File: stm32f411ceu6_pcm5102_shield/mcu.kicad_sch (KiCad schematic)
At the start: 25 parts, among them J3 Conn_01x04_Pin, J4 Conn_01x04_Pin, SW1 RotaryEncoder_Switch_MP

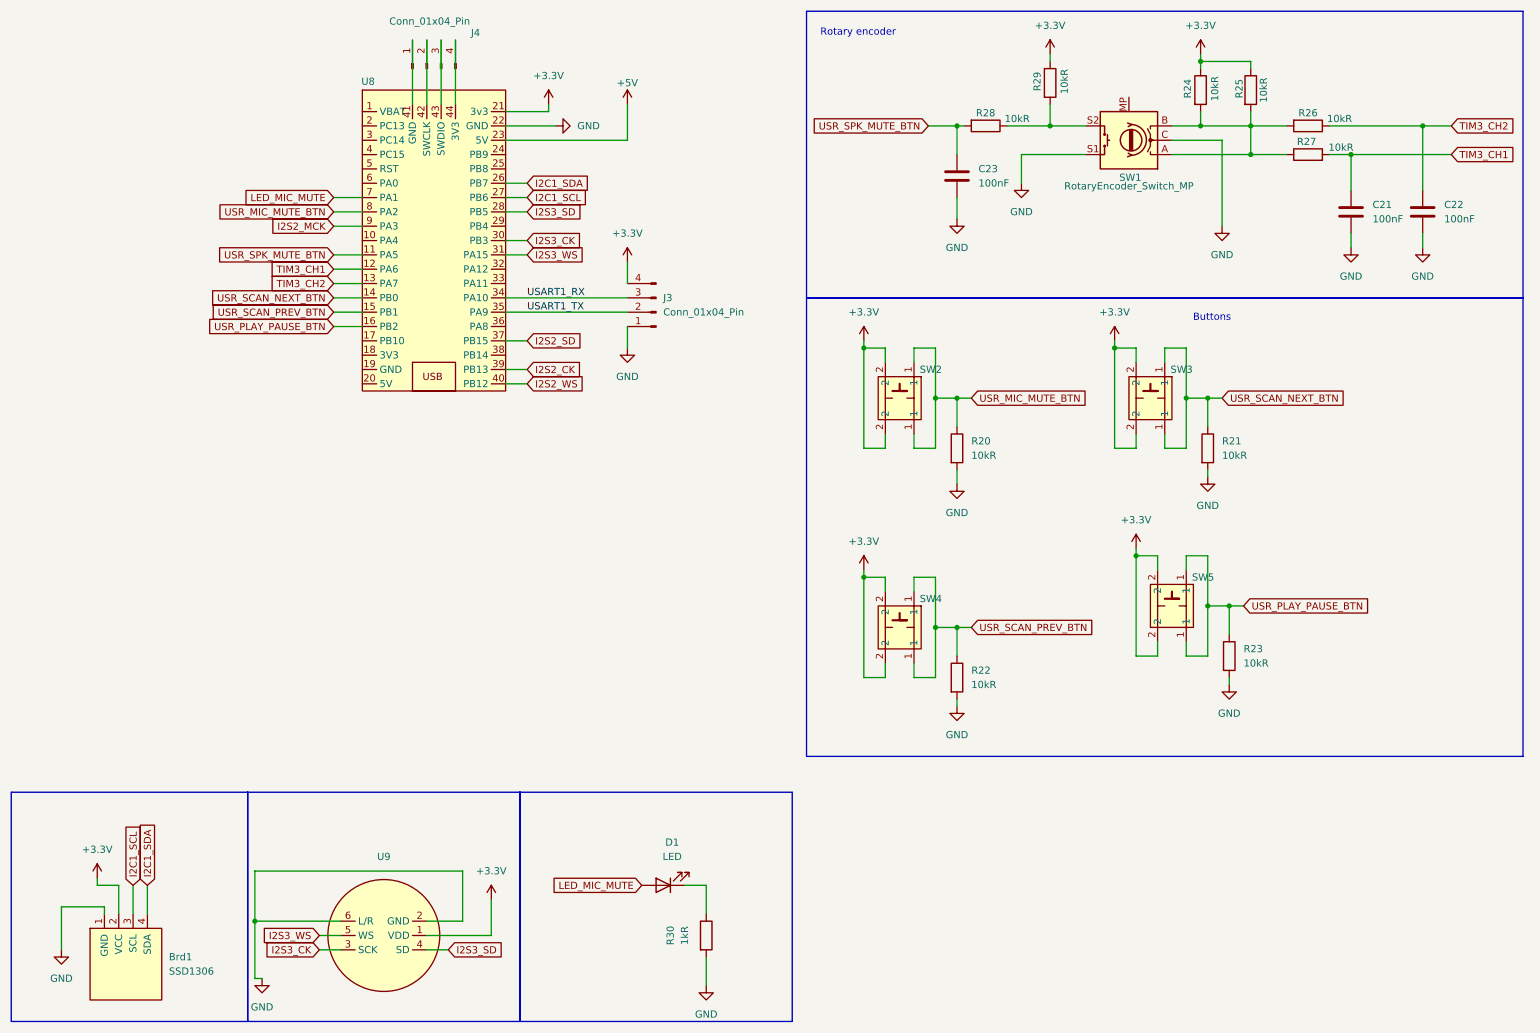
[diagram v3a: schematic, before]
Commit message: Items numeration fix
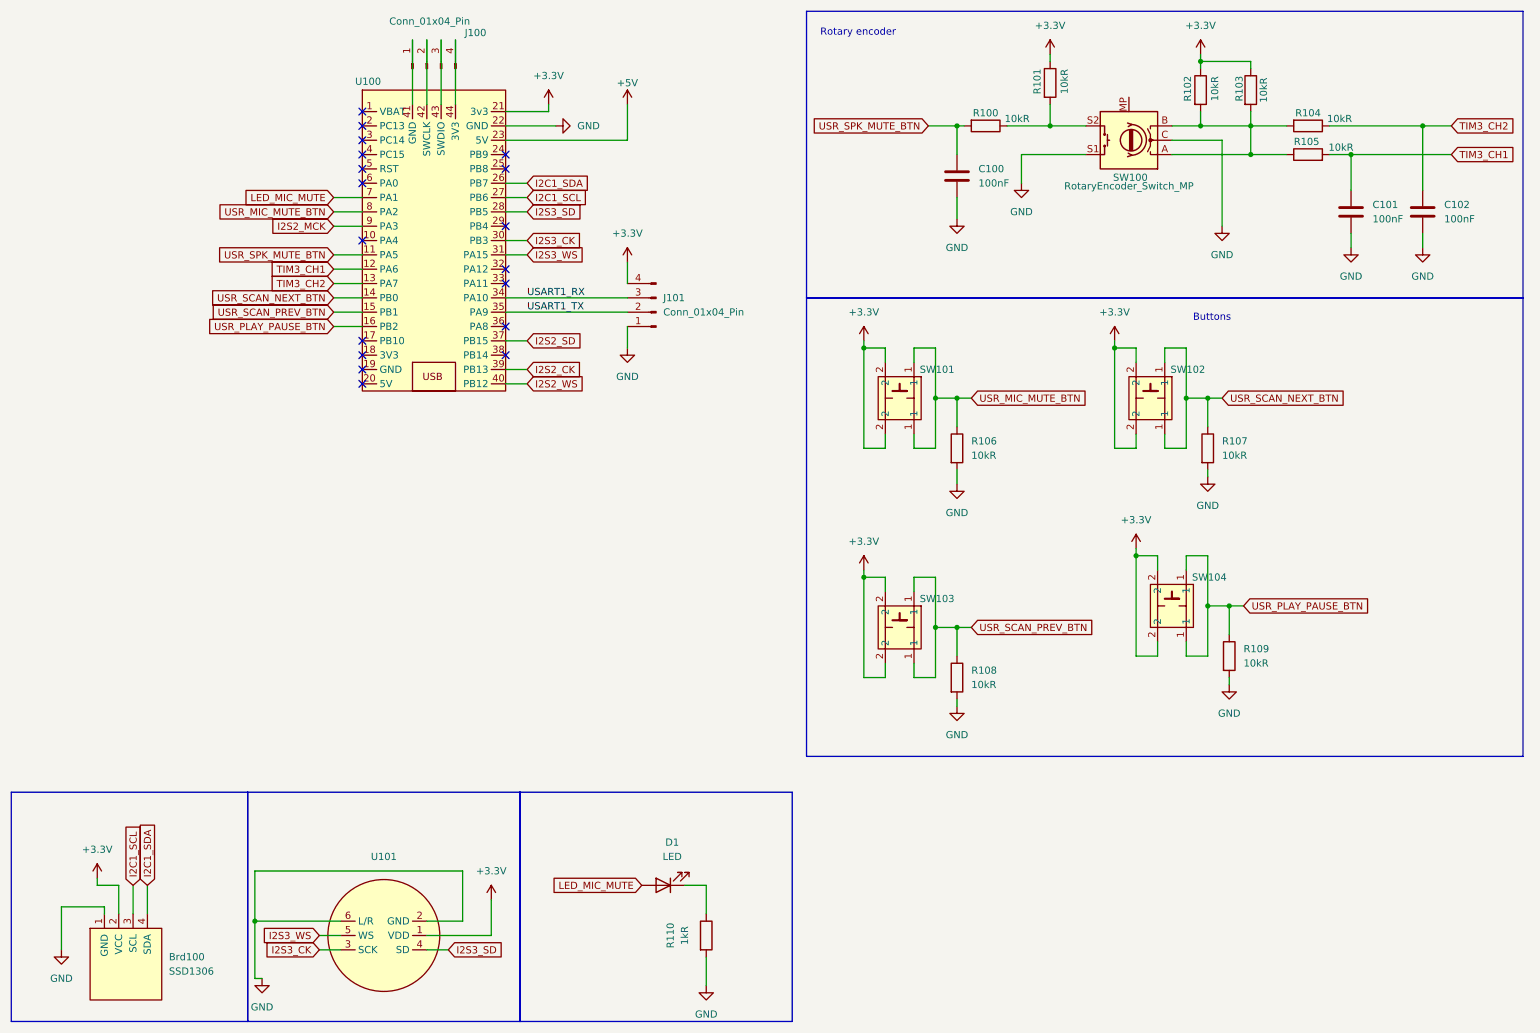
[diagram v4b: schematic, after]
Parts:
- renumbered Brd1 to Brd100, C23 to C100, C21 to C101, C22 to C102, J4 to J100, J3 to J101, R28 to R100, R29 to R101, R24 to R102, R25 to R103, R26 to R104, R27 to R105, R20 to R106, R21 to R107, R22 to R108, R23 to R109, R30 to R110, SW1 to SW100, SW2 to SW101, SW3 to SW102, SW4 to SW103, SW5 to SW104, U8 to U100, U9 to U101
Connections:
- no-connect marks 0 -> 18
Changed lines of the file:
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@@
 		(color 0 0 0 0)
 	)
+	(no_connect
+		(at 74.93 40.64)
+	)
+	(no_connect
+		(at 74.93 78.74)
+	)
+	(no_connect
+		(at 100.33 63.5)
+	)
+	(no_connect
+		(at 74.93 81.28)
+	)
+	(no_connect
+		(at 100.33 60.96)
+	)
+	(no_connect
+		(at 74.93 76.2)
+	)
+	(no_connect
+		(at 74.93 55.88)
+	)
+	(no_connect
+		(at 74.93 35.56)
+	)
+	(no_connect
+		(at 100.33 71.12)
+	)
+	(no_connect
+		(at 74.93 43.18)
+	)
+	(no_connect
+		(at 100.33 76.2)
+	)
+	(no_connect
+		(at 74.93 45.72)
+	)
+	(no_connect
+		(at 74.93 73.66)
+	)
+	(no_connect
+		(at 74.93 33.02)
+	)
+	(no_connect
+		(at 100.33 40.64)
+	)
+	(no_connect
+		(at 100.33 43.18)
+	)
+	(no_connect
+		(at 74.93 38.1)
+	)
+	(no_connect
+		(at 100.33 53.34)
+	)
 	(wire
 		(pts
@@
 		(on_board yes)
 		(dnp no)
-		(property "Reference" "R30"
+		(property "Reference" "R110"
 			(at 129.54 179.07 90)
 			(effects
@@
 			(project "stm32f411ceu6_pcm5102_shield"
 				(path "/aeaad843-2b7c-40e9-bb1d-8d1f5e5d5206/850fb9da-5125-4af4-b1b4-d624ecc42efc"
-					(reference "R30")
+					(reference "R110")
 					(unit 1)
 				)
@@
 		(dnp no)
 		(fields_autoplaced yes)
-		(property "Reference" "R20"
+		(property "Reference" "R106"
 			(at 182.88 91.4399 0)
 			(effects
@@
 			(project "stm32f411ceu6_pcm5102_shield"
 				(path "/aeaad843-2b7c-40e9-bb1d-8d1f5e5d5206/850fb9da-5125-4af4-b1b4-d624ecc42efc"
-					(reference "R20")
+					(reference "R106")
 					(unit 1)
 				)
@@
 		(on_board yes)
 		(dnp no)
-		(property "Reference" "SW4"
+		(property "Reference" "SW103"
 			(at 173.736 119.38 90)
 			(effects
@@
 			(project "stm32f411ceu6_pcm5102_shield"
 				(path "/aeaad843-2b7c-40e9-bb1d-8d1f5e5d5206/850fb9da-5125-4af4-b1b4-d624ecc42efc"
-					(reference "SW4")
+					(reference "SW103")
 					(unit 1)
 				)
@@
 		(on_board yes)
 		(dnp no)
-		(property "Reference" "SW3"
+		(property "Reference" "SW102"
 			(at 218.186 78.74 90)
 			(effects
@@
 			(project "stm32f411ceu6_pcm5102_shield"
 				(path "/aeaad843-2b7c-40e9-bb1d-8d1f5e5d5206/850fb9da-5125-4af4-b1b4-d624ecc42efc"
-					(reference "SW3")
+					(reference "SW102")
 					(unit 1)
 				)
@@
 		(on_board yes)
 		(dnp no)
-		(property "Reference" "J4"
+		(property "Reference" "J100"
 			(at 94.996 19.05 90)
 			(effects
@@
 			(project "stm32f411ceu6_pcm5102_shield"
 				(path "/aeaad843-2b7c-40e9-bb1d-8d1f5e5d5206/850fb9da-5125-4af4-b1b4-d624ecc42efc"
-					(reference "J4")
+					(reference "J100")
 					(unit 1)
 				)
@@
 		(on_board yes)
 		(dnp no)
-		(property "Reference" "U8"
+		(property "Reference" "U100"
 			(at 75.946 27.686 0)
 			(effects
@@
 			(project ""
 				(path "/aeaad843-2b7c-40e9-bb1d-8d1f5e5d5206/850fb9da-5125-4af4-b1b4-d624ecc42efc"
-					(reference "U8")
+					(reference "U100")
 					(unit 1)
 				)
@@
 		(on_board yes)
 		(dnp no)
-		(property "Reference" "R27"
+		(property "Reference" "R105"
 			(at 242.316 38.354 90)
 			(effects
@@
 			(project "stm32f411ceu6_pcm5102_shield"
 				(path "/aeaad843-2b7c-40e9-bb1d-8d1f5e5d5206/850fb9da-5125-4af4-b1b4-d624ecc42efc"
-					(reference "R27")
+					(reference "R105")
 					(unit 1)
 				)
@@
 		(on_board yes)
 		(dnp no)
-		(property "Reference" "SW1"
+		(property "Reference" "SW100"
 			(at 211.074 44.704 0)
 			(effects
@@
 			(project ""
 				(path "/aeaad843-2b7c-40e9-bb1d-8d1f5e5d5206/850fb9da-5125-4af4-b1b4-d624ecc42efc"
-					(reference "SW1")
+					(reference "SW100")
 					(unit 1)
 				)
@@
 		(on_board yes)
 		(dnp no)
-		(property "Reference" "C23"
+		(property "Reference" "C100"
 			(at 184.15 43.18 0)
 			(effects
@@
 			(project "stm32f411ceu6_pcm5102_shield"
 				(path "/aeaad843-2b7c-40e9-bb1d-8d1f5e5d5206/850fb9da-5125-4af4-b1b4-d624ecc42efc"
-					(reference "C23")
+					(reference "C100")
 					(unit 1)
 				)
@@
 		(dnp no)
 		(fields_autoplaced yes)
-		(property "Reference" "R22"
+		(property "Reference" "R108"
 			(at 182.88 132.0799 0)
 			(effects
@@
 			(project "stm32f411ceu6_pcm5102_shield"
 				(path "/aeaad843-2b7c-40e9-bb1d-8d1f5e5d5206/850fb9da-5125-4af4-b1b4-d624ecc42efc"
-					(reference "R22")
+					(reference "R108")
 					(unit 1)
 				)
@@
 		(on_board yes)
 		(dnp no)
-		(property "Reference" "R25"
+		(property "Reference" "R103"
 			(at 230.378 28.956 90)
 			(effects
@@
 			(project "stm32f411ceu6_pcm5102_shield"
 				(path "/aeaad843-2b7c-40e9-bb1d-8d1f5e5d5206/850fb9da-5125-4af4-b1b4-d624ecc42efc"
-					(reference "R25")
+					(reference "R103")
 					(unit 1)
 				)
@@
 		(on_board yes)
 		(dnp no)
-		(property "Reference" "R29"
+		(property "Reference" "R101"
 			(at 194.564 27.686 90)
 			(effects
@@
 			(project "stm32f411ceu6_pcm5102_shield"
 				(path "/aeaad843-2b7c-40e9-bb1d-8d1f5e5d5206/850fb9da-5125-4af4-b1b4-d624ecc42efc"
-					(reference "R29")
+					(reference "R101")
 					(unit 1)
 				)
@@
 		(on_board yes)
 		(dnp no)
-		(property "Reference" "C21"
+		(property "Reference" "C101"
 			(at 254 49.53 0)
 			(effects
@@
 			(project "stm32f411ceu6_pcm5102_shield"
 				(path "/aeaad843-2b7c-40e9-bb1d-8d1f5e5d5206/850fb9da-5125-4af4-b1b4-d624ecc42efc"
-					(reference "C21")
+					(reference "C101")
 					(unit 1)
 				)
@@
 		(dnp no)
 		(fields_autoplaced yes)
-		(property "Reference" "J3"
+		(property "Reference" "J101"
 			(at 128.27 66.0399 0)
 			(effects
@@
 			(project ""
 				(path "/aeaad843-2b7c-40e9-bb1d-8d1f5e5d5206/850fb9da-5125-4af4-b1b4-d624ecc42efc"
-					(reference "J3")
+					(reference "J101")
 					(unit 1)
 				)
@@
 		(on_board yes)
 		(dnp no)
-		(property "Reference" "R28"
+		(property "Reference" "R100"
 			(at 185.42 33.274 90)
 			(effects
@@
 			(project "stm32f411ceu6_pcm5102_shield"
 				(path "/aeaad843-2b7c-40e9-bb1d-8d1f5e5d5206/850fb9da-5125-4af4-b1b4-d624ecc42efc"
-					(reference "R28")
+					(reference "R100")
 					(unit 1)
 				)
@@
 		(on_board yes)
 		(dnp no)
-		(property "Reference" "SW2"
+		(property "Reference" "SW101"
 			(at 173.736 78.74 90)
 			(effects
@@
 			(project "stm32f411ceu6_pcm5102_shield"
 				(path "/aeaad843-2b7c-40e9-bb1d-8d1f5e5d5206/850fb9da-5125-4af4-b1b4-d624ecc42efc"
-					(reference "SW2")
+					(reference "SW101")
 					(unit 1)
 				)
@@
 		(dnp no)
 		(fields_autoplaced yes)
-		(property "Reference" "Brd1"
+		(property "Reference" "Brd100"
 			(at 40.64 182.8799 0)
 			(effects
@@
 			(project ""
 				(path "/aeaad843-2b7c-40e9-bb1d-8d1f5e5d5206/850fb9da-5125-4af4-b1b4-d624ecc42efc"
-					(reference "Brd1")
+					(reference "Brd100")
 					(unit 1)
 				)
@@
 		(dnp no)
 		(fields_autoplaced yes)
-		(property "Reference" "R23"
+		(property "Reference" "R109"
 			(at 231.14 128.2699 0)
 			(effects
@@
 			(project "stm32f411ceu6_pcm5102_shield"
 				(path "/aeaad843-2b7c-40e9-bb1d-8d1f5e5d5206/850fb9da-5125-4af4-b1b4-d624ecc42efc"
-					(reference "R23")
+					(reference "R109")
 					(unit 1)
 				)
@@
 		(dnp no)
 		(fields_autoplaced yes)
-		(property "Reference" "U9"
+		(property "Reference" "U101"
 			(at 78.74 165.1 0)
 			(effects
@@
 			(project ""
 				(path "/aeaad843-2b7c-40e9-bb1d-8d1f5e5d5206/850fb9da-5125-4af4-b1b4-d624ecc42efc"
-					(reference "U9")
+					(reference "U101")
 					(unit 1)
 				)
@@
 		(on_board yes)
 		(dnp no)
-		(property "Reference" "R26"
+		(property "Reference" "R104"
 			(at 242.57 33.274 90)
 			(effects
@@
 			(project "stm32f411ceu6_pcm5102_shield"
 				(path "/aeaad843-2b7c-40e9-bb1d-8d1f5e5d5206/850fb9da-5125-4af4-b1b4-d624ecc42efc"
-					(reference "R26")
+					(reference "R104")
 					(unit 1)
 				)
@@
 		(dnp no)
 		(fields_autoplaced yes)
-		(property "Reference" "R21"
+		(property "Reference" "R107"
 			(at 227.33 91.4399 0)
 			(effects
@@
 			(project "stm32f411ceu6_pcm5102_shield"
 				(path "/aeaad843-2b7c-40e9-bb1d-8d1f5e5d5206/850fb9da-5125-4af4-b1b4-d624ecc42efc"
-					(reference "R21")
+					(reference "R107")
 					(unit 1)
 				)
@@
 		(on_board yes)
 		(dnp no)
-		(property "Reference" "R24"
+		(property "Reference" "R102"
 			(at 221.234 28.956 90)
 			(effects
@@
 			(project "stm32f411ceu6_pcm5102_shield"
 				(path "/aeaad843-2b7c-40e9-bb1d-8d1f5e5d5206/850fb9da-5125-4af4-b1b4-d624ecc42efc"
-					(reference "R24")
+					(reference "R102")
 					(unit 1)
 				)
@@
 	)
 	(symbol
+		(lib_name "BlackPillLibrary:SW_PUSH_6mm_H5mm")
 		(lib_id "BlackPillLibrary:SW_PUSH_6mm_H5mm")
 		(at 219.71 120.65 270)
@@
 		(on_board yes)
 		(dnp no)
-		(property "Reference" "SW5"
+		(property "Reference" "SW104"
 			(at 221.996 115.57 90)
 			(effects
@@
 			(project "stm32f411ceu6_pcm5102_shield"
 				(path "/aeaad843-2b7c-40e9-bb1d-8d1f5e5d5206/850fb9da-5125-4af4-b1b4-d624ecc42efc"
-					(reference "SW5")
+					(reference "SW104")
 					(unit 1)
 				)
@@
 		(on_board yes)
 		(dnp no)
-		(property "Reference" "C22"
+		(property "Reference" "C102"
 			(at 266.7 49.53 0)
 			(effects
@@
 			(project "stm32f411ceu6_pcm5102_shield"
 				(path "/aeaad843-2b7c-40e9-bb1d-8d1f5e5d5206/850fb9da-5125-4af4-b1b4-d624ecc42efc"
-					(reference "C22")
+					(reference "C102")
 					(unit 1)
 				)

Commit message: BOM updates
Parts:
- C100, C101, C102: Manufacturer Samwha Capacitor -> Samsung Electro-Mechanics; Manufacturer Part Number CS2012X5R226M160NRE -> CL21B104KBCNNNC
- R100, R101, R102, R103, R104, R105: Manufacturer Part Number 0805W8F100JT5E -> 0805W8J0103T5E
- R106, R107, R108, R109: footprint Resistor_SMD:R_0402_1005Metric -> Resistor_SMD:R_0805_2012Metric; Manufacturer Part Number (none) -> 0805W8J0103T5E
- R110: Manufacturer Part Number 0805W8F100JT5E -> 0805W8F1001T5E
- SW100: Aliexpress link (none) -> https://www.aliexpress.com/item/1005006160663514.html
- U100: value ~ -> BlackPill
- U101: value ~ -> INMP411
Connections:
- no-connect marks 18 -> 19
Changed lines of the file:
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@@
 	)
 	(no_connect
+		(at 210.82 30.48)
+	)
+	(no_connect
 		(at 100.33 60.96)
 	)
@@
 			)
 		)
-		(property "Manufacturer Part Number" "0805W8F100JT5E"
+		(property "Manufacturer Part Number" "0805W8F1001T5E"
 			(at 135.89 179.07 0)
 			(effects
@@
 	)
 	(symbol
-		(lib_id "power:+5V")
-		(at 121.92 31.75 0)
-		(unit 1)
-		(exclude_from_sim no)
-		(in_bom yes)
-		(on_board yes)
-		(dnp no)
-		(property "Reference" "#PWR063"
-			(at 121.92 35.56 0)
-			(effects
-				(font
-					(size 1.27 1.27)
-				)
-				(hide yes)
-			)
-		)
-		(property "Value" "+5V"
-			(at 121.92 27.94 0)
-			(effects
-				(font
-					(size 1.27 1.27)
-				)
-			)
-		)
-		(property "Footprint" ""
-			(at 121.92 31.75 0)
-			(effects
-				(font
-					(size 1.27 1.27)
-				)
-				(hide yes)
-			)
-		)
-		(property "Datasheet" ""
-			(at 121.92 31.75 0)
-			(effects
-				(font
-					(size 1.27 1.27)
-				)
-				(hide yes)
-			)
-		)
-		(property "Description" ""
-			(at 121.92 31.75 0)
-			(effects
-				(font
-					(size 1.27 1.27)
-				)
-				(hide yes)
-			)
-		)
-		(pin "1"
-		)
-		(instances
-			(project "stm32f411ceu6_pcm5102_shield"
-				(path "/aeaad843-2b7c-40e9-bb1d-8d1f5e5d5206/850fb9da-5125-4af4-b1b4-d624ecc42efc"
-					(reference "#PWR063")
-					(unit 1)
-				)
-			)
-		)
-	)
-	(symbol
 		(lib_id "power:+3.3V")
 		(at 208.28 73.66 0)
@@
 			)
 		)
-		(property "Footprint" "Resistor_SMD:R_0402_1005Metric"
+		(property "Footprint" "Resistor_SMD:R_0805_2012Metric"
 			(at 178.562 92.71 90)
 			(effects
@@
 			)
 		)
+		(property "Manufacturer Part Number" "0805W8J0103T5E"
+			(at 180.34 92.71 0)
+			(effects
+				(font
+					(size 1.27 1.27)
+				)
+				(hide yes)
+			)
+		)
 		(pin "1"
 		)
@@
 			)
 		)
-		(property "Value" "~"
+		(property "Value" "BlackPill"
 			(at 87.63 27.94 0)
 			(effects
@@
 			)
 		)
-		(property "Manufacturer Part Number" "0805W8F100JT5E"
+		(property "Manufacturer Part Number" "0805W8J0103T5E"
 			(at 242.57 40.64 0)
 			(effects
@@
 			)
 		)
+		(property "Aliexpress link" "https://www.aliexpress.com/item/1005006160663514.html"
+			(at 210.82 38.1 0)
+			(effects
+				(font
+					(size 1.27 1.27)
+				)
+				(hide yes)
+			)
+		)
 		(pin "S1"
 		)
@@
 			)
 		)
-		(property "Manufacturer" "Samwha Capacitor"
+		(property "Manufacturer" "Samsung Electro-Mechanics"
 			(at 180.34 44.45 0)
 			(effects
@@
 			)
 		)
-		(property "Manufacturer Part Number" "CS2012X5R226M160NRE"
+		(property "Manufacturer Part Number" "CL21B104KBCNNNC"
 			(at 180.34 44.45 0)
 			(effects
@@
 			)
 		)
-		(property "Footprint" "Resistor_SMD:R_0402_1005Metric"
+		(property "Footprint" "Resistor_SMD:R_0805_2012Metric"
 			(at 178.562 133.35 90)
 			(effects
@@
 			)
 		)
+		(property "Manufacturer Part Number" "0805W8J0103T5E"
+			(at 180.34 133.35 0)
+			(effects
+				(font
+					(size 1.27 1.27)
+				)
+				(hide yes)
+			)
+		)
 		(pin "1"
 		)
@@
 			)
 		)
-		(property "Manufacturer Part Number" "0805W8F100JT5E"
+		(property "Manufacturer Part Number" "0805W8J0103T5E"
 			(at 232.41 29.21 0)
 			(effects
@@
 	)
 	(symbol
+		(lib_id "power:+5V")
+		(at 121.92 31.75 0)
+		(unit 1)
+		(exclude_from_sim no)
+		(in_bom yes)
+		(on_board yes)
+		(dnp no)
+		(fields_autoplaced yes)
+		(property "Reference" "#PWR063"
+			(at 121.92 35.56 0)
+			(effects
+				(font
+					(size 1.27 1.27)
+				)
+				(hide yes)
+			)
+		)
+		(property "Value" "+5V"
+			(at 121.92 26.67 0)
+			(effects
+				(font
+					(size 1.27 1.27)
+				)
+			)
+		)
+		(property "Footprint" ""
+			(at 121.92 31.75 0)
+			(effects
+				(font
+					(size 1.27 1.27)
+				)
+				(hide yes)
+			)
+		)
+		(property "Datasheet" ""
+			(at 121.92 31.75 0)
+			(effects
+				(font
+					(size 1.27 1.27)
+				)
+				(hide yes)
+			)
+		)
+		(property "Description" "Power symbol creates a global label with name \"+5V\""
+			(at 121.92 31.75 0)
+			(effects
+				(font
+					(size 1.27 1.27)
+				)
+				(hide yes)
+			)
+		)
+		(pin "1"
+		)
+		(instances
+			(project "stm32f411ceu6_pcm5102_shield"
+				(path "/aeaad843-2b7c-40e9-bb1d-8d1f5e5d5206/850fb9da-5125-4af4-b1b4-d624ecc42efc"
+					(reference "#PWR063")
+					(unit 1)
+				)
+			)
+		)
+	)
+	(symbol
 		(lib_id "Device:R")
 		(at 196.85 27.94 0)
@@
 			)
 		)
-		(property "Manufacturer Part Number" "0805W8F100JT5E"
+		(property "Manufacturer Part Number" "0805W8J0103T5E"
 			(at 196.85 27.94 0)
 			(effects
@@
 			)
 		)
-		(property "Manufacturer" "Samwha Capacitor"
+		(property "Manufacturer" "Samsung Electro-Mechanics"
 			(at 250.19 50.8 0)
 			(effects
@@
 			)
 		)
-		(property "Manufacturer Part Number" "CS2012X5R226M160NRE"
+		(property "Manufacturer Part Number" "CL21B104KBCNNNC"
 			(at 250.19 50.8 0)
 			(effects
@@
 			)
 		)
-		(property "Manufacturer Part Number" "0805W8F100JT5E"
+		(property "Manufacturer Part Number" "0805W8J0103T5E"
 			(at 185.42 35.56 0)
 			(effects
@@
 			)
 		)
-		(property "Footprint" "Resistor_SMD:R_0402_1005Metric"
+		(property "Footprint" "Resistor_SMD:R_0805_2012Metric"
 			(at 226.822 129.54 90)
 			(effects
@@
 			)
 		)
+		(property "Manufacturer Part Number" "0805W8J0103T5E"
+			(at 228.6 129.54 0)
+			(effects
+				(font
+					(size 1.27 1.27)
+				)
+				(hide yes)
+			)
+		)
 		(pin "1"
 		)
@@
 			)
 		)
-		(property "Value" "~"
+		(property "Value" "INMP411"
 			(at 78.74 167.64 0)
 			(effects
@@
 			)
 		)
-		(property "Manufacturer Part Number" "0805W8F100JT5E"
+		(property "Manufacturer Part Number" "0805W8J0103T5E"
 			(at 242.57 35.56 0)
 			(effects
@@
 			)
 		)
-		(property "Footprint" "Resistor_SMD:R_0402_1005Metric"
+		(property "Footprint" "Resistor_SMD:R_0805_2012Metric"
 			(at 223.012 92.71 90)
 			(effects
@@
 			)
 		)
+		(property "Manufacturer Part Number" "0805W8J0103T5E"
+			(at 224.79 92.71 0)
+			(effects
+				(font
+					(size 1.27 1.27)
+				)
+				(hide yes)
+			)
+		)
 		(pin "1"
 		)
@@
 			)
 		)
-		(property "Manufacturer Part Number" "0805W8F100JT5E"
+		(property "Manufacturer Part Number" "0805W8J0103T5E"
 			(at 223.52 29.21 0)
 			(effects
@@
 			)
 		)
-		(property "Manufacturer" "Samwha Capacitor"
+		(property "Manufacturer" "Samsung Electro-Mechanics"
 			(at 262.89 50.8 0)
 			(effects
@@
 			)
 		)
-		(property "Manufacturer Part Number" "CS2012X5R226M160NRE"
+		(property "Manufacturer Part Number" "CL21B104KBCNNNC"
 			(at 262.89 50.8 0)
 			(effects
